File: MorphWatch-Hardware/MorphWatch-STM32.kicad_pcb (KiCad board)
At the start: 4 copper layers, 33.8 x 46 mm, 64 parts, among them IC1 ME6211C33M5G-N, J1 USB, J2 Conn_01x24, J3 Conn_01x04, J4 Conn_01x02, J5 Conn_01x05, M1 Motor_DC_ALT, Q1 CJ2301_S1, Q2 DMN3042L, Q3 S8050, U1 TP4054, U2 STM32L476RGTx, U3 JDY-08, U4 MPU-6050, Y1 Crystal_GND24

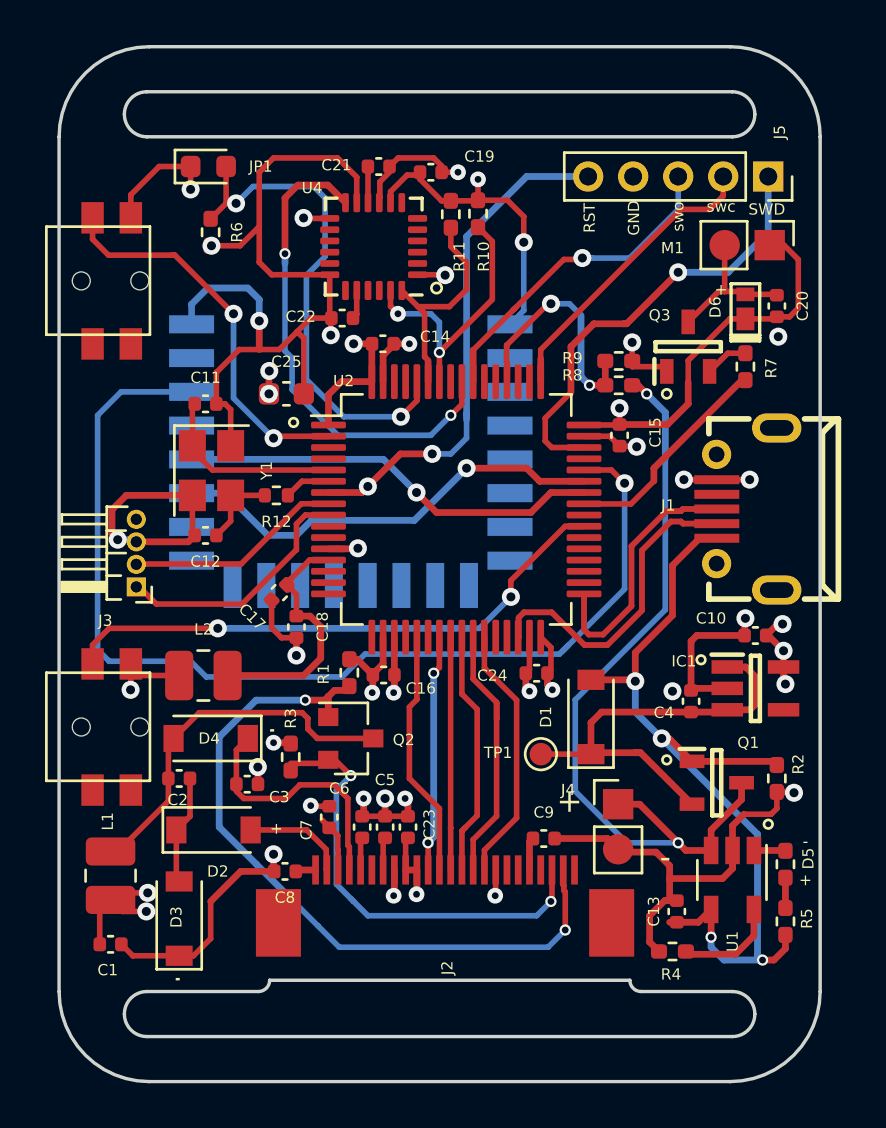
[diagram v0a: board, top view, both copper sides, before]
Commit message: Updated Board to satisfy DRC
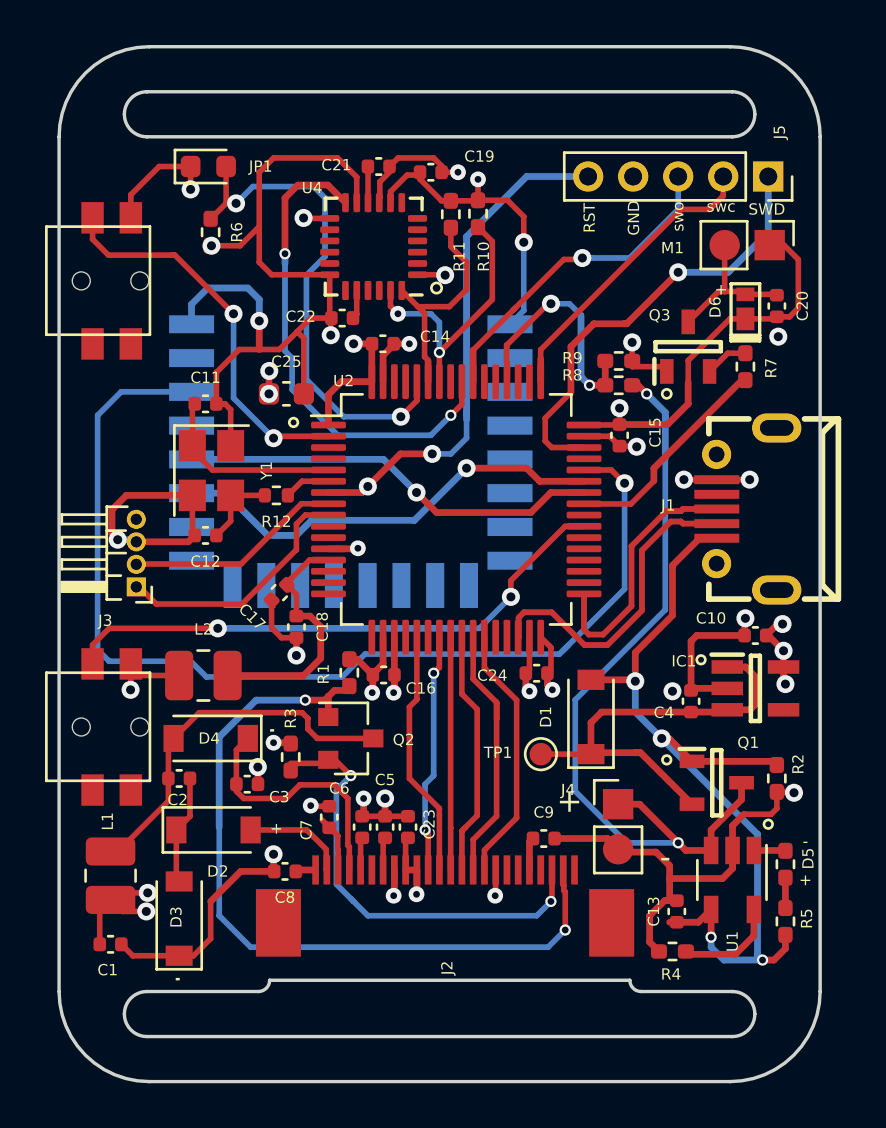
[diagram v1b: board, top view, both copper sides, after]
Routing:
- net GDR: track 32.3 -> 34.6 mm
- net GND: track 124.9 -> 124.1 mm, vias 27 -> 26
